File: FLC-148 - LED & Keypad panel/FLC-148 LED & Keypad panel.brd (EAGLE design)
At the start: 52 x 73.8 mm, 75 parts, among them IC1 MAX6818, IC2 MAX6818, IC3 NTGD3148NT1G, IC4 NTGD3148NT1G, IC5 STM32G071CBU6, IC6 ECS-480-10-33B-CKM-TR, J1 FTSH-107-01-L-DV-K-A

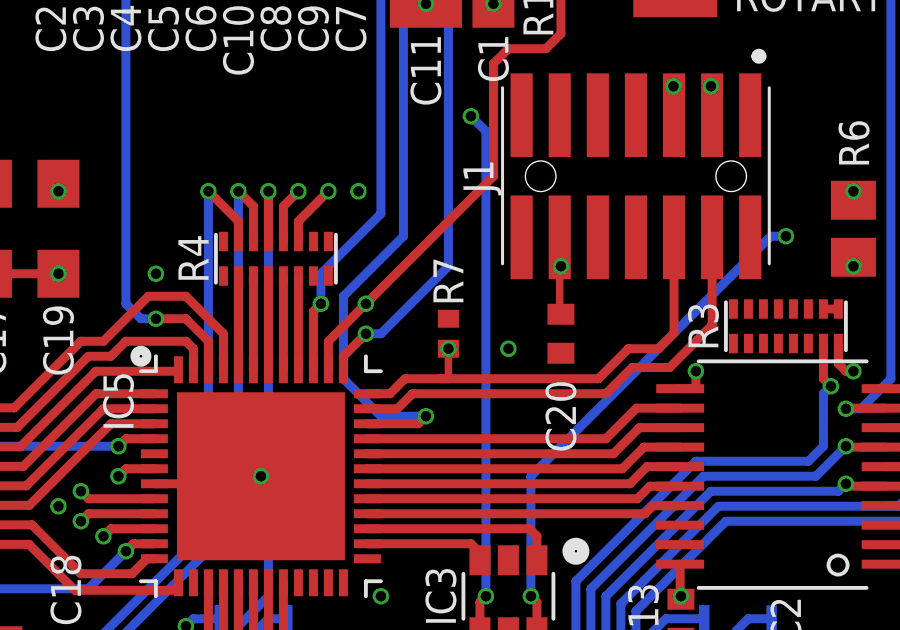
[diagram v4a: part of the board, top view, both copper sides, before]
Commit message: - removed R7 (swdclk to gnd), since it is not needed
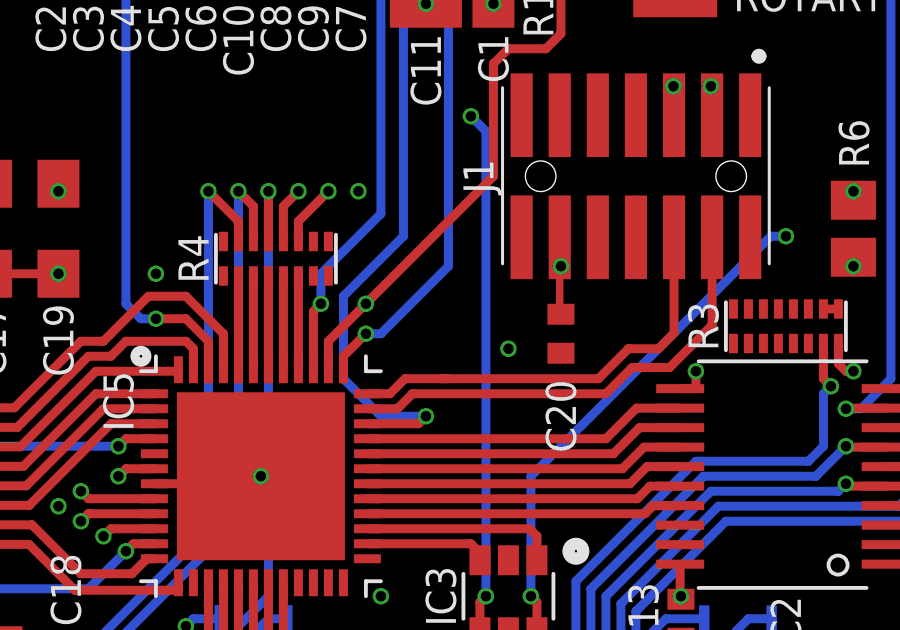
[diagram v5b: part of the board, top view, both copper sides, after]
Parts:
- removed R7: 10k, rcl:R0402
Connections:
- net GND: no longer R7.1
- net SWDCLK: no longer R7.2
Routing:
- net SWDCLK: track 65.8 -> 64.8 mm, vias 2 -> 1

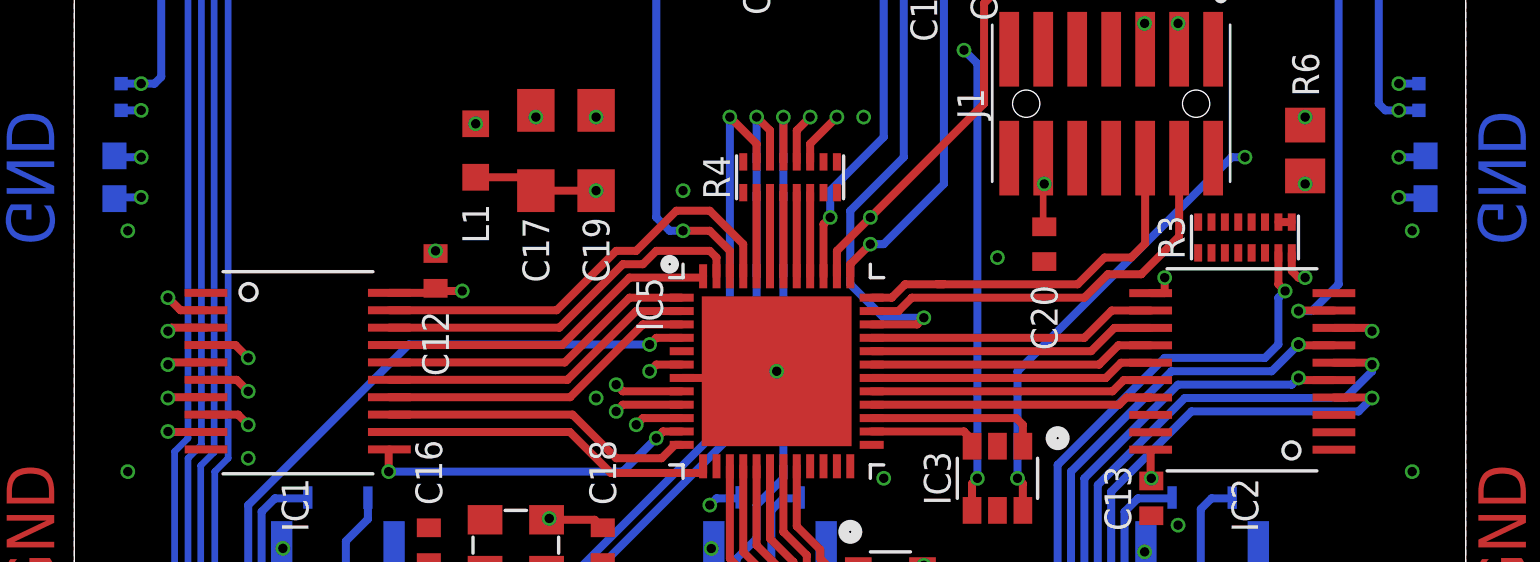
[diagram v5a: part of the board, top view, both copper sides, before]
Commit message: - connected rotary encoder A and B out directly to micro controller (previously these lines were going through the debouncing IC)
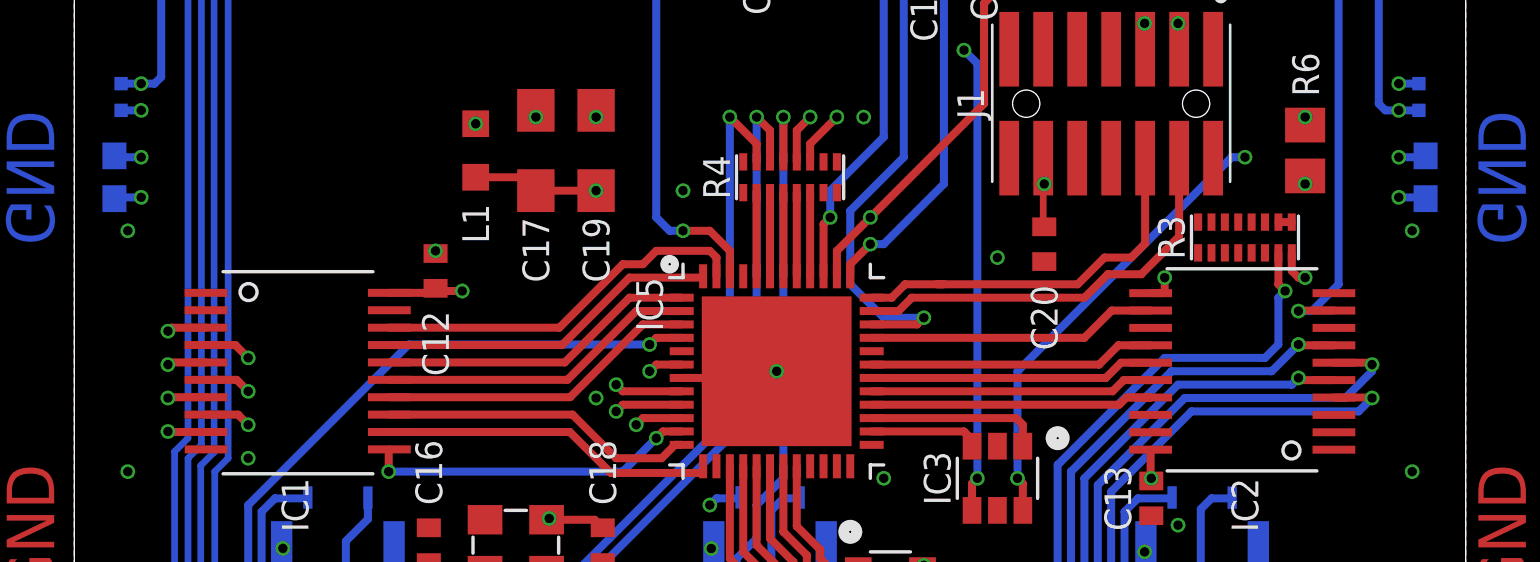
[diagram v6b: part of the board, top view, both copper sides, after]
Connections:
- removed net ROTARY_A_OUT: IC2.OUT7, IC5.32_PA10
- removed net ROTARY_B_OUT: IC1.OUT1, IC5.45_PB6
- net ROTARY_A_IN: now also IC5.32_PA10; no longer IC2.IN7
- net ROTARY_B_IN: now also IC5.45_PB6; no longer IC1.IN1
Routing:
- net ROTARY_B_IN: track 45.4 -> 21.6 mm, vias 2 -> 1
- net ROTARY_B_OUT: track 16.5 -> 0.00 mm
- net ROTARY_A_IN: track 25.6 -> 13.1 mm, vias 2 -> 1
- net ROTARY_A_OUT: track 10.8 -> 0.00 mm
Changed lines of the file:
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@@
 <layers>
 <layer number="1" name="Top" color="4" fill="1" visible="yes" active="yes"/>
-<layer number="2" name="Route2" color="16" fill="1" visible="no" active="yes"/>
+<layer number="2" name="Route2" color="16" fill="1" visible="yes" active="yes"/>
 <layer number="3" name="Route3" color="17" fill="1" visible="no" active="no"/>
 <layer number="4" name="Route4" color="18" fill="1" visible="no" active="no"/>
@@
 <layer number="13" name="Route13" color="21" fill="1" visible="no" active="no"/>
 <layer number="14" name="Route14" color="22" fill="1" visible="no" active="no"/>
-<layer number="15" name="Route15" color="23" fill="1" visible="no" active="yes"/>
-<layer number="16" name="Bottom" color="1" fill="1" visible="no" active="yes"/>
+<layer number="15" name="Route15" color="23" fill="1" visible="yes" active="yes"/>
+<layer number="16" name="Bottom" color="1" fill="1" visible="yes" active="yes"/>
 <layer number="17" name="Pads" color="2" fill="1" visible="yes" active="yes"/>
 <layer number="18" name="Vias" color="2" fill="1" visible="yes" active="yes"/>
@@
 <layer number="20" name="Dimension" color="24" fill="1" visible="yes" active="yes"/>
 <layer number="21" name="tPlace" color="7" fill="1" visible="yes" active="yes"/>
-<layer number="22" name="bPlace" color="7" fill="1" visible="no" active="yes"/>
+<layer number="22" name="bPlace" color="7" fill="1" visible="yes" active="yes"/>
 <layer number="23" name="tOrigins" color="15" fill="1" visible="yes" active="yes"/>
-<layer number="24" name="bOrigins" color="15" fill="1" visible="no" active="yes"/>
-<layer number="25" name="tNames" color="7" fill="1" visible="yes" active="yes"/>
+<layer number="24" name="bOrigins" color="15" fill="1" visible="yes" active="yes"/>
+<layer number="25" name="tNames" color="7" fill="1" visible="no" active="yes"/>
 <layer number="26" name="bNames" color="7" fill="1" visible="no" active="yes"/>
 <layer number="27" name="tValues" color="7" fill="1" visible="no" active="yes"/>
 <layer number="28" name="bValues" color="7" fill="1" visible="no" active="yes"/>
-<layer number="29" name="tStop" color="7" fill="3" visible="yes" active="yes"/>
+<layer number="29" name="tStop" color="7" fill="3" visible="no" active="yes"/>
 <layer number="30" name="bStop" color="7" fill="6" visible="no" active="yes"/>
 <layer number="31" name="tCream" color="7" fill="4" visible="no" active="yes"/>
@@
 <layer number="38" name="bTest" color="7" fill="1" visible="no" active="yes"/>
 <layer number="39" name="tKeepout" color="4" fill="11" visible="yes" active="yes"/>
-<layer number="40" name="bKeepout" color="1" fill="11" visible="no" active="yes"/>
+<layer number="40" name="bKeepout" color="1" fill="11" visible="yes" active="yes"/>
 <layer number="41" name="tRestrict" color="4" fill="10" visible="yes" active="yes"/>
-<layer number="42" name="bRestrict" color="1" fill="10" visible="no" active="yes"/>
+<layer number="42" name="bRestrict" color="1" fill="10" visible="yes" active="yes"/>
 <layer number="43" name="vRestrict" color="2" fill="10" visible="yes" active="yes"/>
 <layer number="44" name="Drills" color="7" fill="1" visible="no" active="yes"/>
@@
 <layer number="50" name="dxf" color="7" fill="1" visible="no" active="no"/>
 <layer number="51" name="tDocu" color="7" fill="1" visible="yes" active="yes"/>
-<layer number="52" name="bDocu" color="7" fill="1" visible="no" active="yes"/>
+<layer number="52" name="bDocu" color="7" fill="1" visible="yes" active="yes"/>
 <layer number="53" name="tGND_GNDA" color="7" fill="1" visible="no" active="no"/>
 <layer number="54" name="bGND_GNDA" color="7" fill="1" visible="no" active="no"/>
@@
 <signal name="ROTARY_B_IN" class="2">
 <contactref element="ROTARY" pad="4"/>
-<contactref element="IC1" pad="IN1"/>
-<via x="3.5" y="35.5" extent="1-16" drill="0.35"/>
-<wire x1="4.925" y1="35.03" x2="3.97" y2="35.03" width="0.3" layer="1"/>
-<wire x1="3.97" y1="35.03" x2="3.5" y2="35.5" width="0.3" layer="1"/>
 <via x="38.25" y="55.25" extent="1-16" drill="0.35"/>
 <wire x1="37.71" y1="55.25" x2="38.25" y2="55.25" width="0.3" layer="1"/>
-<wire x1="3.5" y1="35.5" x2="3.5" y2="36" width="0.4" layer="15"/>
-<wire x1="3.5" y1="36" x2="18.85" y2="51.35" width="0.4" layer="15"/>
 <wire x1="36.55" y1="55.25" x2="38.25" y2="55.25" width="0.4" layer="15"/>
 <wire x1="36.55" y1="55.25" x2="32.65" y2="51.35" width="0.4" layer="15"/>
 <wire x1="32.65" y1="51.35" x2="18.85" y2="51.35" width="0.4" layer="15"/>
-</signal>
-<signal name="ROTARY_A_OUT" class="2">
-<contactref element="IC2" pad="OUT7"/>
-<contactref element="IC5" pad="32_PA10"/>
-<wire x1="29.8" y1="33.5" x2="38" y2="33.5" width="0.3" layer="1"/>
-<wire x1="38" y1="33.5" x2="38.87" y2="34.37" width="0.3" layer="1"/>
-<wire x1="38.87" y1="34.37" x2="40.225" y2="34.37" width="0.3" layer="1"/>
+<contactref element="IC5" pad="45_PB6"/>
+<wire x1="25" y1="36.3" x2="18.85" y2="51.35" width="0" layer="19" extent="1-15"/>
 </signal>
 <signal name="SBATT" class="1">
@@
 <wire x1="30.25" y1="12.5" x2="30.25" y2="18.96" width="0.3" layer="1"/>
 </signal>
-<signal name="ROTARY_B_OUT" class="2">
-<contactref element="IC1" pad="OUT1"/>
-<contactref element="IC5" pad="45_PB6"/>
-<wire x1="25" y1="37.5" x2="25" y2="36.3" width="0.3" layer="1"/>
-<wire x1="23.75" y1="38.75" x2="25" y2="37.5" width="0.3" layer="1"/>
-<wire x1="11.775" y1="35.03" x2="18.03" y2="35.03" width="0.3" layer="1"/>
-<wire x1="18.03" y1="35.03" x2="20.25" y2="37.25" width="0.3" layer="1"/>
-<wire x1="20.25" y1="37.25" x2="21" y2="37.25" width="0.3" layer="1"/>
-<wire x1="21" y1="37.25" x2="22.5" y2="38.75" width="0.3" layer="1"/>
-<wire x1="22.5" y1="38.75" x2="23.75" y2="38.75" width="0.3" layer="1"/>
-</signal>
 <signal name="ROTARY_A_IN" class="2">
 <contactref element="ROTARY" pad="2"/>
-<contactref element="IC2" pad="IN7"/>
-<via x="48.5" y="34.25" extent="1-16" drill="0.35"/>
-<wire x1="47.075" y1="34.37" x2="48.38" y2="34.37" width="0.3" layer="1"/>
-<wire x1="48.38" y1="34.37" x2="48.5" y2="34.25" width="0.3" layer="1"/>
 <via x="38.25" y="53.25" extent="1-16" drill="0.35"/>
 <wire x1="37.71" y1="53.25" x2="38.25" y2="53.25" width="0.3" layer="1"/>
 <wire x1="47.25" y1="44.75" x2="38.75" y2="53.25" width="0.4" layer="15"/>
 <wire x1="38.25" y1="53.25" x2="38.75" y2="53.25" width="0.4" layer="15"/>
-<wire x1="48.5" y1="36.25" x2="48.5" y2="34.25" width="0.4" layer="15"/>
-<wire x1="48.5" y1="36.25" x2="47.25" y2="37.5" width="0.4" layer="15"/>
-<wire x1="47.25" y1="44.75" x2="47.25" y2="37.5" width="0.4" layer="15"/>
+<contactref element="IC5" pad="32_PA10"/>
+<wire x1="29.8" y1="33.5" x2="47.25" y2="44.75" width="0" layer="19" extent="1-15"/>
 </signal>
 <signal name="ROTARY_PUSH_OUT" class="2">

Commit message: - more todo updates - added ground vias
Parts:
- moved LCD 0.25 mm to (26.0, 55.5)
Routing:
- net N$6: track 0.00 -> 1.00 mm, vias 0 -> 1
- net CP3: track 90.4 -> 91.4 mm
- net CP1: track 65.9 -> 66.8 mm
- net GND: track 6.45 -> 6.37 mm, vias 55 -> 63
